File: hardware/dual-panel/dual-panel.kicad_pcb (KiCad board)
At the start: 4 copper layers, 210.9 x 127 mm, 174 parts, among them J201 FSR West, J202 FSR South, J203 FSR East, J204 RS-485 IN, J205 12V_IN, J206 FSR North, J207 RS-485 OUT, J208 12V_OUT, J209 SWD, J210 Conn_01x08_Pin, J211 Conn_01x08_Pin, J212 Conn_01x08_Pin, J213 Conn_01x08_Pin, J214 INT OUT, J301 Conn_01x08_Socket, J302 Conn_01x08_Socket, J303 Conn_01x08_Socket, J304 Conn_01x08_Socket, J305 USB_C_Receptacle_USB2.0_16P, SW201 PANEL_ID, SW202 RS-485 Termination, SW301 BOOTSEL, U301 SN74AHCT1G125, U302 AP7361C-33ER-13, U303 AMS1117-5.0, U304 LM66200, U305 USBLC6-2SC6, U306 RP2040, U307 W25Q32JV, U308 THVD1429, X301 12MHz ABM8-272-T3

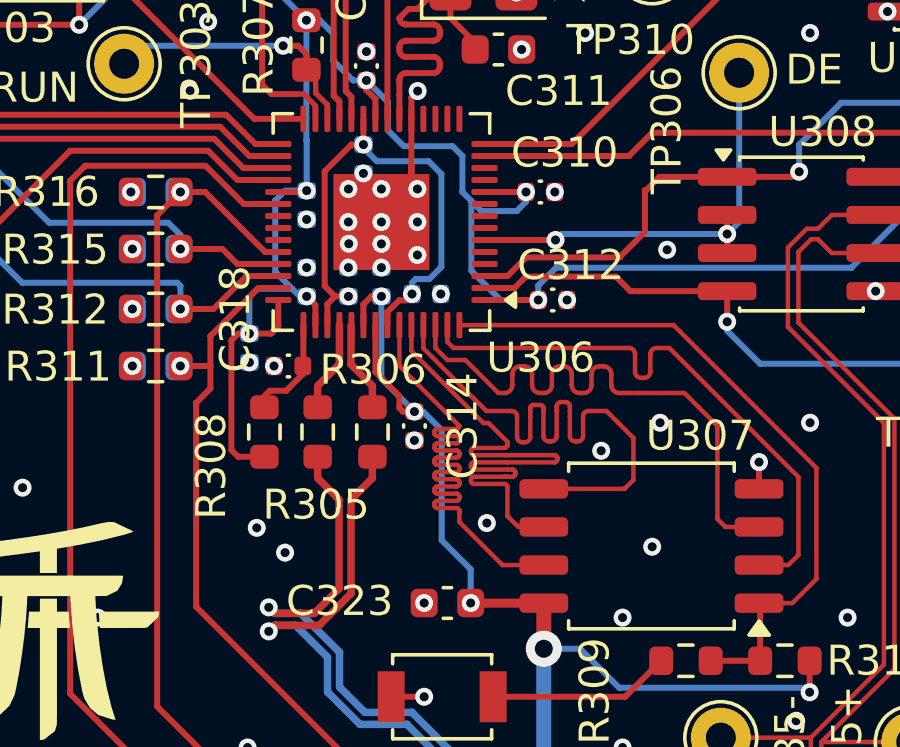
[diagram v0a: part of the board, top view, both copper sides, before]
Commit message: dru: hold the GND pour off the QSPI flash bus, scoped to those nets
JLC's trace-spacing Danger on the flash serpentine survived two rounds of
re-routing, because re-routing was never going to fix it. The 0.09mm gap is
between the serpentine and the surrounding GND POUR, not between traces: the
blanket "Minimum Trace Width and Spacing" rule permits 0.09mm, so the pour
refills to exactly that no matter how the traces are moved. Measured before this
change, QSPI trace-to-trace was already up at 0.14mm while QSPI-to-pour sat at
0.0905-0.0918mm across seven spots.

Fixed with a clearance rule scoped to the six QSPI nets rather than a board-wide
increase. Board-wide was tried earlier and rejected: every value above 0.09mm --
0.10, 0.11, 0.12, 0.125 -- orphans a copper island near J211 and produces a
starved_thermal. Scoping it to QSPI avoids that entirely, since the affected pour
is all on the brain.

0.13mm is the largest value the existing routing satisfies. At 0.15mm seven
track-to-track and track-to-pad pairs fail, tightest 0.1314mm, and those a refill
cannot resolve. At 0.13mm the board is clean with no starved_thermal, and nothing
touching a QSPI net remains under 0.15mm -- the pour backed off from every flash
trace.

Also verified after the user's RP2040 thermal-via moves that the POFV facts in
ORDER_NOTES.md still hold exactly: 83 via-in-pad instances, 17 under U306, none
above the 0.5mm fill limit. Board clean at baseline, zone fills current, panel
and fab package regenerated.
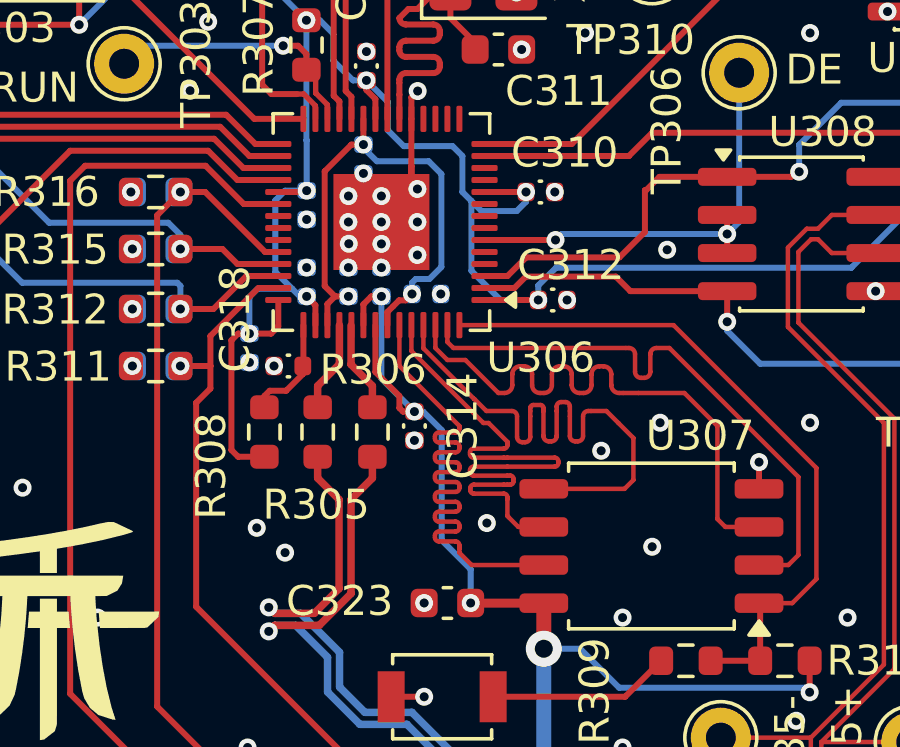
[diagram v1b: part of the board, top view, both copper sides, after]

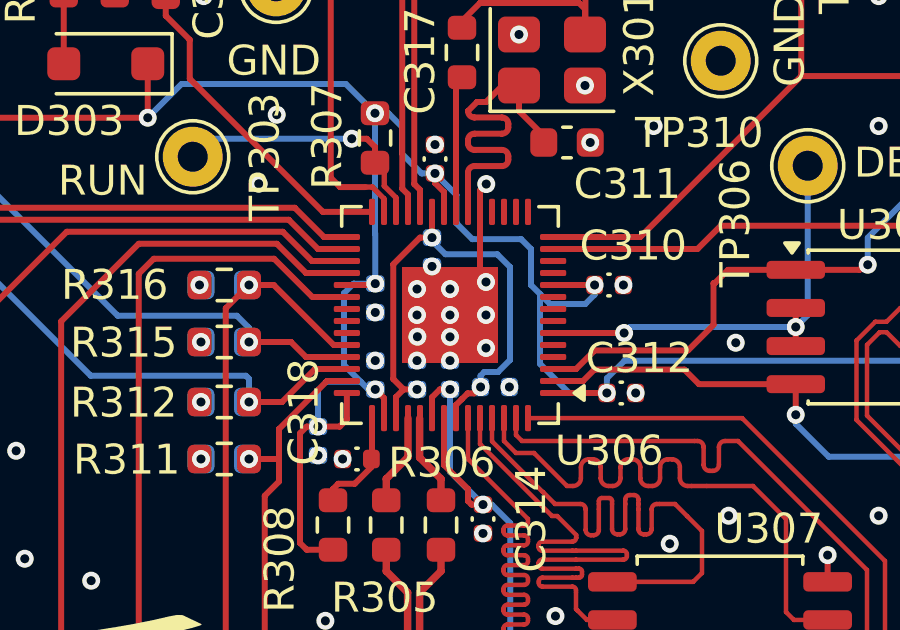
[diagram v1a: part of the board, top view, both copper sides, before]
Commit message: rev1: order both boards, and freeze exactly what went to fab
Boards are at JLCPCB as of 2026-08-18. Everything after this commit is rev 2.

Four design changes made on order day, all verified before submitting:

- U306 RP2040 signal pads 0.20 -> 0.23 mm, matching Raspberry Pi's official
  land pattern, via a local footprint. Length/pitch/centres/EP unchanged.
  Needed a zone refill and scoping the QSPI pour rule to B.Type == 'Zone'
  (it had no B-side condition, so it was policing track-to-pad too).
- RS-485 transceiver THVD1429 -> THVD1450DR on BOTH boards. Identical SOIC-8
  pinout. Gives up on-die IEC 61000-4-5 surge, which TI scopes to lightning and
  power-grid transients; gains 18 kV vs 8 kV contact ESD, the threat this pad
  actually documents. Also -$52 and 84x the stock, retiring the BOM's tightest
  line (60 units).
- 10 nF ADC filter caps C57112 -> C723749. The old part was X7R while the
  schematic said C0G; these are the four FSR ADC inputs, where Class II's
  piezoelectric response would inject charge synchronously with a footstep.
  Found by auditing all 35 BOM lines against live LCSC pages.
- master-pcb: 297 vias 0.45 -> 0.60 mm (0.075 -> 0.150 mm annular), after
  running DFM on the master for the first time. A quote is not a DFM check.

Both boards re-verified after every change: dual-panel 0/19/90/0,
master 0/0/0/0.

Adds hardware/fab-archive/rev1-2026-08-18/ with the byte-exact artifacts that
were manufactured, plus SHA256SUMS and a .gitattributes that disables CRLF
normalisation so they stay byte-exact. hardware/**/production/ is gitignored,
so without this there would be no record in git of what was physically built.

Adds QUOTE-2026-08-18.md (the real qty-20 quote; the July one is now marked
superseded) and splits the JLC order notes into PCB and PCBA remark blocks,
each within the 500-character limit the order form imposes.
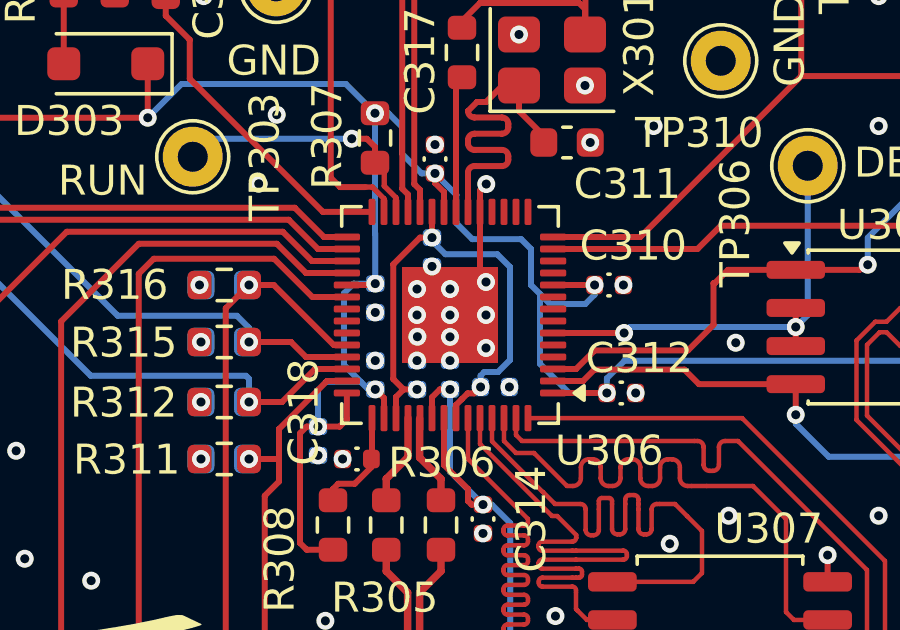
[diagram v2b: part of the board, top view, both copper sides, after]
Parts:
- C304, C305, C319, C320: value 1uF X5R 16V -> 1uF X5R 25V
- C324, C326, C329, C330: value 10nF C0G 50V -> 10nF C0G 25V
- U306: footprint Package_DFN_QFN:QFN-56-1EP_7x7mm_P0.4mm_EP3.2x3.2mm -> dual-panel:QFN-56-1EP_7x7mm_P0.4mm_EP3.2x3.2mm_RPiPad
- U308: value THVD1429 -> THVD1450
